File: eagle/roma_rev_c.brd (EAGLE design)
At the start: 49 x 41 mm, 23 parts, among them IC1 78L12, U1 LTC3426

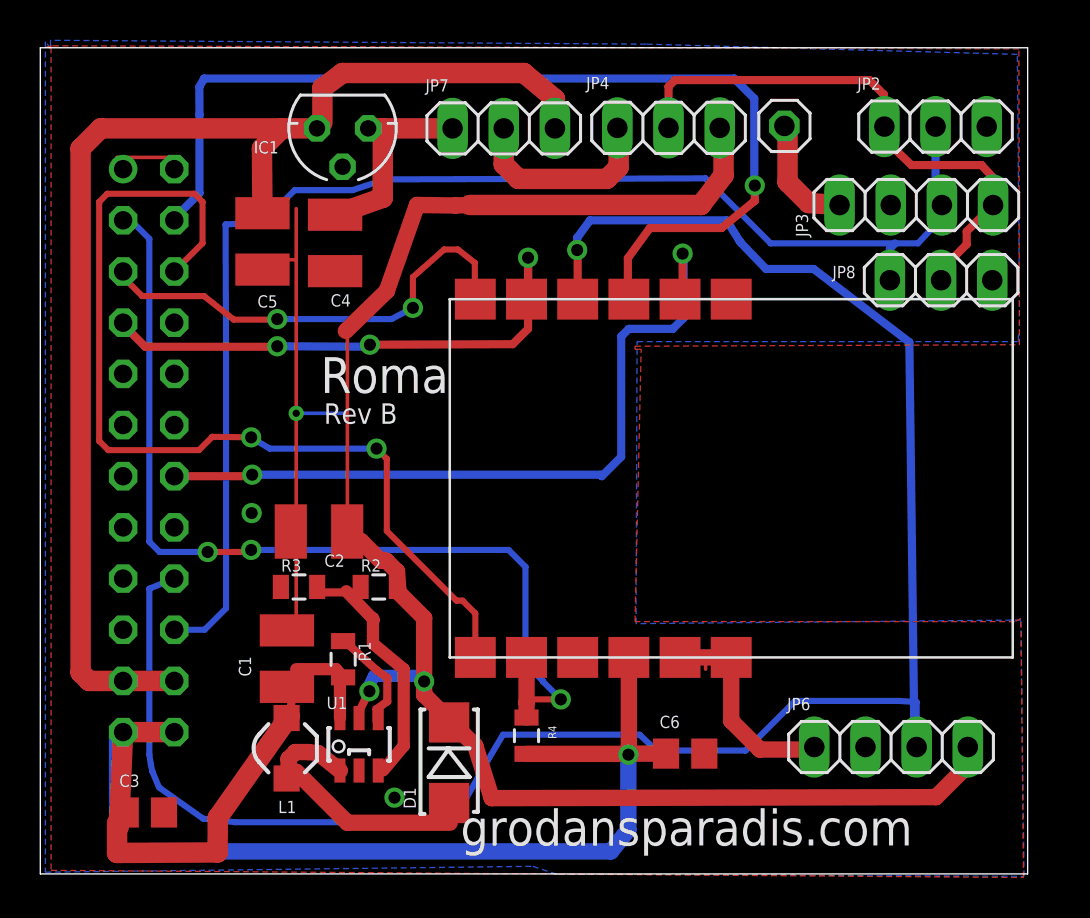
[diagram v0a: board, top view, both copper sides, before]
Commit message: JP4 should be numbered the other way around. Added descriptive text.
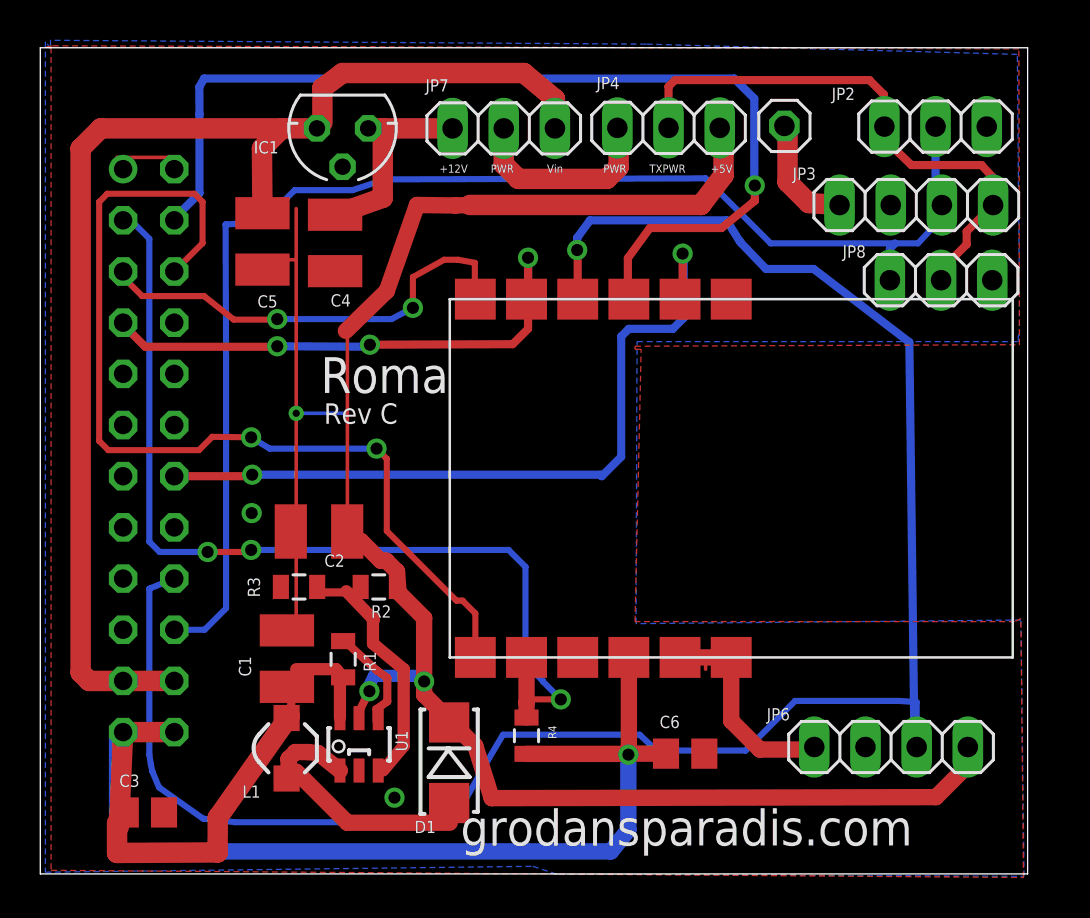
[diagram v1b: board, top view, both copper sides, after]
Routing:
- net SCK1: track 22.8 -> 22.2 mm
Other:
- board text added: "+12V"
- board text added: "+5V"
- board text added: "PWR"
- board text added: "Rev C"
- board text added: "TXPWR"
- board text added: "Vin"
- board text removed: "Rev B"

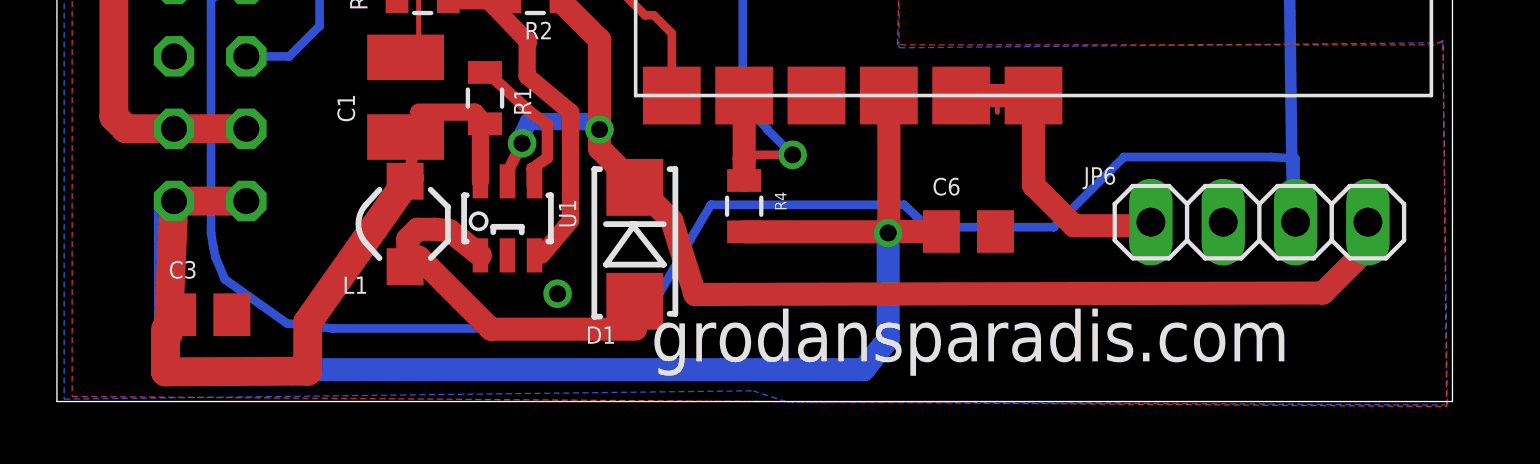
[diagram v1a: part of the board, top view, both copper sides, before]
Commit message: Added solder short to get +5V from Odessa 5V without converter.
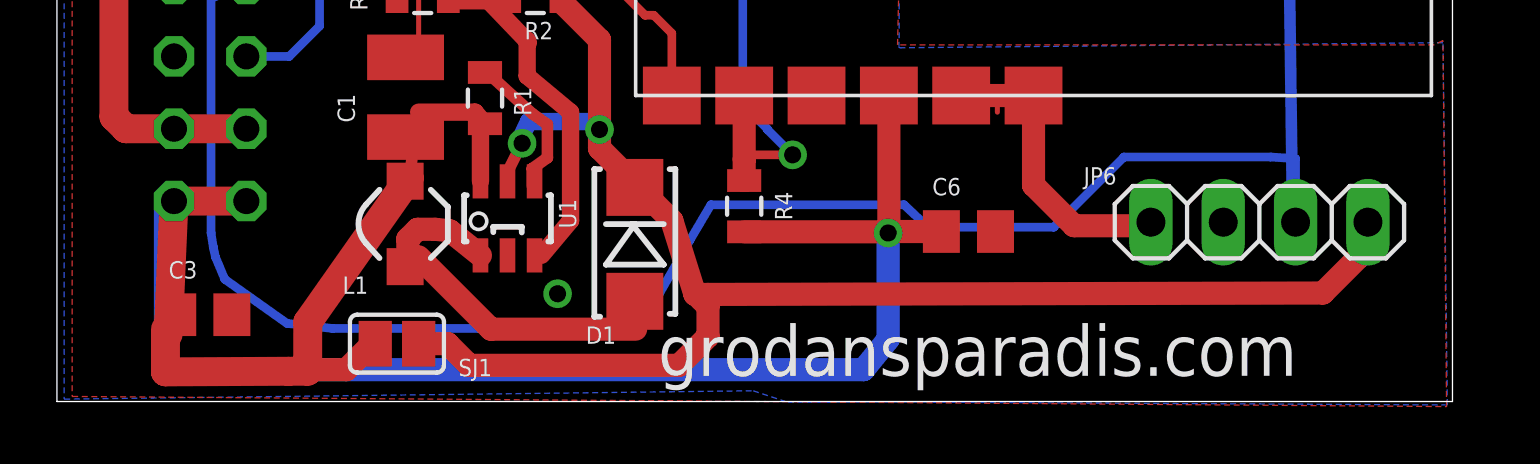
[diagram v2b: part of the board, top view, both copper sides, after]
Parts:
- added SJ1: (no value), jumper:SJ
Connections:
- net +3V3: now also SJ1.1
- net +5V: now also SJ1.2
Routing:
- net +5V: track 82.8 -> 95.8 mm
- net +3V3: track 77.9 -> 81.3 mm
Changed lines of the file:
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@@
 <plain>
 <text x="14.0759" y="22.339" size="1.016" layer="25" font="fixed">Rev C</text>
-<text x="20.8556" y="1.41" size="1.778" layer="25" font="fixed">grodansparadis.com</text>
+<text x="21.1096" y="0.902" size="1.778" layer="25" font="fixed">grodansparadis.com</text>
 <text x="13.9129" y="23.8682" size="1.778" layer="25" font="fixed">Roma</text>
 <wire x1="0" y1="0" x2="0" y2="41" width="0" layer="20"/>
@@
 <element name="U$1" library="eurosource_mrf24j40ma" package="MRF24J40MA" value="MRF24J40MA" x="27.94" y="19.6342" smashed="yes" rot="R270"/>
 <element name="R4" library="CH_passive" package="0805" value="10K" x="24.13" y="6.858" smashed="yes" rot="R270">
-<attribute name="NAME" x="25.2095" y="7.366" size="0.4064" layer="25" rot="R270"/>
+<attribute name="NAME" x="25.2095" y="7.366" size="0.6096" layer="25" rot="R270"/>
 </element>
 <element name="C6" library="rcl" package="C0805" value="100n" x="32.004" y="5.969" smashed="yes">
@@
 <attribute name="NAME" x="40.9702" y="31.1912" size="0.6096" layer="25" ratio="10" rot="R180"/>
 <attribute name="VALUE" x="40.894" y="26.289" size="1.27" layer="27"/>
+</element>
+<element name="SJ1" library="jumper" package="SJ" value="" x="11.938" y="2.032" smashed="yes">
+<attribute name="NAME" x="14.097" y="0.889" size="0.6096" layer="25" ratio="10"/>
+<attribute name="VALUE" x="12.3381" y="2.032" size="0.02" layer="27"/>
 </element>
 </elements>
@@
 <wire x1="8.8065" y1="2.7863" x2="12.3698" y2="7.8486" width="1.016" layer="1"/>
 <wire x1="8.8019" y1="1.0651" x2="8.8065" y2="2.7863" width="1.016" layer="1"/>
-<wire x1="3.81" y1="1.0413" x2="8.8019" y2="1.0651" width="1.016" layer="1"/>
+<wire x1="3.81" y1="1.0413" x2="8.12778125" y2="1.0618875" width="1.016" layer="1"/>
+<wire x1="8.12778125" y1="1.0618875" x2="8.8019" y2="1.0651" width="1.016" layer="1"/>
 <wire x1="3.81" y1="2.54" x2="3.81" y2="1.0413" width="1.016" layer="1"/>
 <wire x1="12.3698" y1="7.8486" x2="12.2249" y2="7.7357" width="1.016" layer="1"/>
@@
 <wire x1="24.13" y1="5.958" x2="29.1448" y2="5.958" width="0.8128" layer="1"/>
 <wire x1="29.1448" y1="5.958" x2="29.1846" y2="5.9182" width="0.8128" layer="1"/>
+<contactref element="SJ1" pad="1"/>
+<wire x1="11.176" y1="2.032" x2="11.0744" y2="2.032" width="0.8128" layer="1"/>
+<wire x1="11.0744" y1="2.032" x2="10.16" y2="1.1176" width="0.8128" layer="1"/>
+<wire x1="10.16" y1="1.1176" x2="8.18349375" y2="1.1176" width="0.8128" layer="1"/>
+<wire x1="8.18349375" y1="1.1176" x2="8.12778125" y2="1.0618875" width="0.8128" layer="1"/>
 </signal>
 <signal name="N$2">
@@
 <wire x1="17.78" y1="13.97" x2="17.697" y2="14.2419" width="0.1778" layer="1"/>
 <wire x1="44.45" y1="3.81" x2="45.72" y2="5.08" width="0.8128" layer="1"/>
-<wire x1="22.4028" y1="3.7592" x2="44.45" y2="3.81" width="0.8128" layer="1"/>
+<wire x1="22.4028" y1="3.7592" x2="22.860115625" y2="3.760253125" width="0.8128" layer="1"/>
+<wire x1="22.860115625" y1="3.760253125" x2="44.45" y2="3.81" width="0.8128" layer="1"/>
 <wire x1="21.59" y1="6.35" x2="22.4028" y2="3.7592" width="0.8128" layer="1"/>
 <wire x1="20.32" y1="7.62" x2="21.59" y2="6.35" width="0.8128" layer="1"/>
@@
 <wire x1="16.2521" y1="8.9193" x2="15.7949" y2="8.01" width="0.4064" layer="1"/>
 <wire x1="15.7949" y1="8.01" x2="15.8203" y2="7.7306" width="0.4064" layer="1"/>
+<contactref element="SJ1" pad="2"/>
+<wire x1="12.7" y1="2.032" x2="13.716" y2="2.032" width="0.8128" layer="1"/>
+<wire x1="13.716" y1="2.032" x2="14.478" y2="1.27" width="0.8128" layer="1"/>
+<wire x1="14.478" y1="1.27" x2="21.844" y2="1.27" width="0.8128" layer="1"/>
+<wire x1="21.844" y1="1.27" x2="22.86" y2="2.286" width="0.8128" layer="1"/>
+<wire x1="22.86" y1="2.286" x2="22.86" y2="3.34369375" width="0.8128" layer="1"/>
+<wire x1="22.86" y1="3.34369375" x2="22.626846875" y2="3.576846875" width="0.8128" layer="1"/>
+<wire x1="22.626846875" y1="3.576846875" x2="22.3837375" y2="3.81995625" width="0.8128" layer="1"/>
+<wire x1="22.86" y1="3.81" x2="22.626846875" y2="3.576846875" width="0.1778" layer="1"/>
+<wire x1="22.86" y1="3.81" x2="22.860115625" y2="3.760253125" width="0.1778" layer="1"/>
 </signal>
 <signal name="N$4">

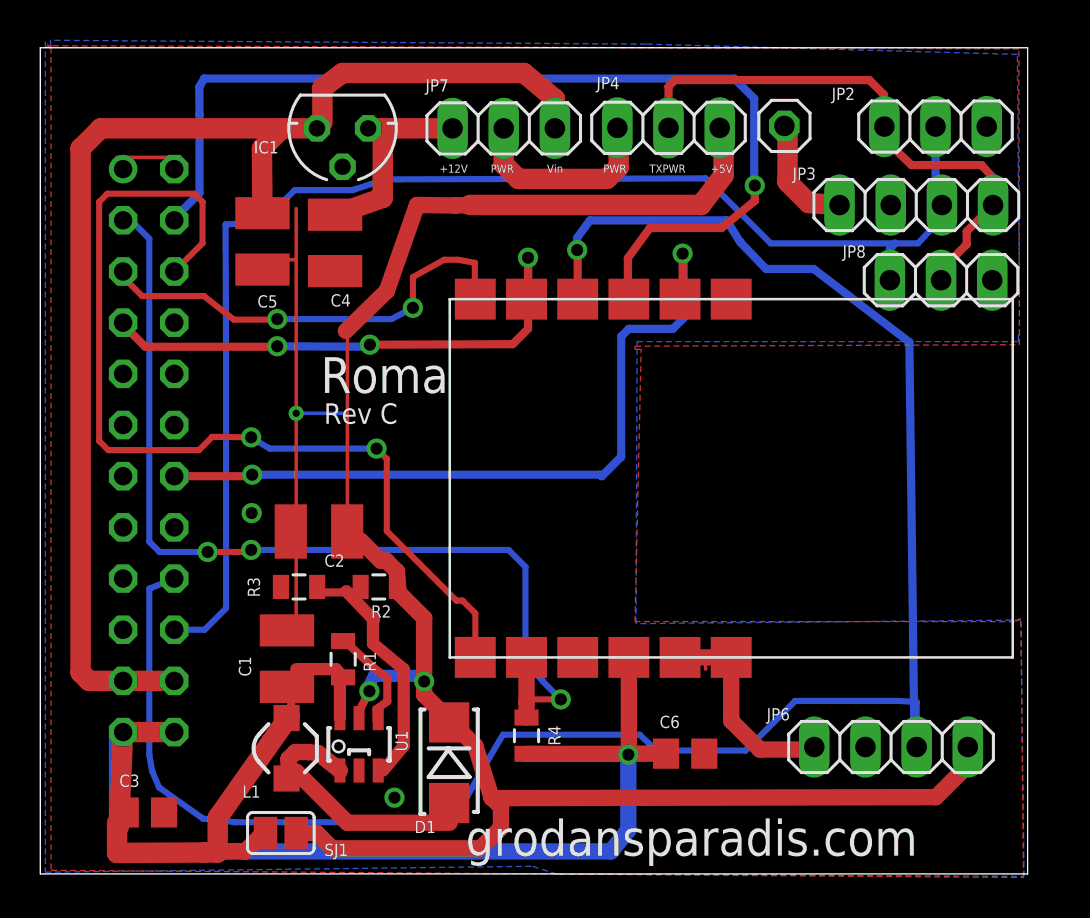
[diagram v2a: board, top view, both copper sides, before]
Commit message: Redrawn signal that goes over transceiver protected zone
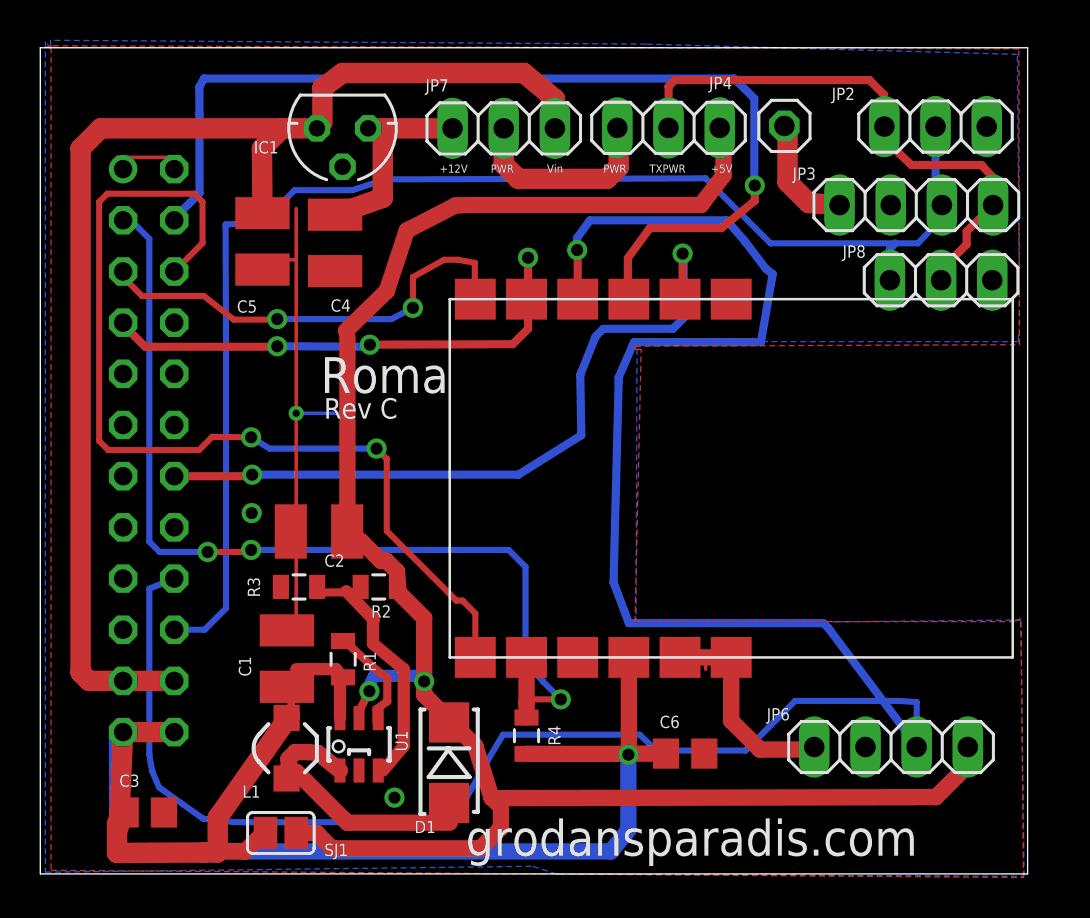
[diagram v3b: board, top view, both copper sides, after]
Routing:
- net RX_433: track 97.9 -> 111.2 mm
- net RESET: track 37.6 -> 36.1 mm
- net +5V: track 95.8 -> 95.2 mm
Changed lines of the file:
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@@
 <board>
 <plain>
-<text x="14.0759" y="22.339" size="1.016" layer="25" font="fixed">Rev C</text>
+<text x="14.0759" y="22.593" size="1.016" layer="25" font="fixed">Rev C</text>
 <text x="21.1096" y="0.902" size="1.778" layer="25" font="fixed">grodansparadis.com</text>
 <text x="13.9129" y="23.8682" size="1.778" layer="25" font="fixed">Roma</text>
@@
 </element>
 <element name="JP4" library="pinhead" package="1X03" value="" x="31.1785" y="37.0242" smashed="yes" rot="R180">
-<attribute name="NAME" x="27.5971" y="38.9472" size="0.6096" layer="25" ratio="10"/>
+<attribute name="NAME" x="33.1851" y="38.9472" size="0.6096" layer="25" ratio="10"/>
 <attribute name="VALUE" x="34.9885" y="40.1992" size="1.27" layer="27" rot="R180"/>
 </element>
@@
 </element>
 <element name="C4" library="CH_passive" package="1210" value="22uF" x="14.6312" y="31.3142" smashed="yes" rot="R270">
-<attribute name="NAME" x="14.4058" y="28.1582" size="0.6096" layer="25"/>
+<attribute name="NAME" x="14.4058" y="27.9042" size="0.6096" layer="25"/>
 </element>
 <element name="C5" library="CH_passive" package="1210" value="10uF" x="11.0254" y="31.3904" smashed="yes" rot="R270">
-<attribute name="NAME" x="10.7736" y="28.1084" size="0.6096" layer="25"/>
+<attribute name="NAME" x="9.7576" y="27.8544" size="0.6096" layer="25"/>
 </element>
 <element name="JP7" library="pinhead" package="1X03" value="" x="23" y="37" smashed="yes">
@@
 <contactref element="JP4" pad="1"/>
 <contactref element="JP6" pad="4"/>
-<wire x1="21.3106" y1="33.1978" x2="32.7914" y2="33.1978" width="1.016" layer="1"/>
-<wire x1="32.7914" y1="33.1978" x2="33.909" y2="34.671" width="1.016" layer="1"/>
-<wire x1="33.909" y1="34.671" x2="33.909" y2="36.8337" width="1.016" layer="1"/>
+<wire x1="21.3106" y1="33.1978" x2="32.7914" y2="33.1978" width="0.8128" layer="1"/>
+<wire x1="32.7914" y1="33.1978" x2="33.909" y2="34.671" width="0.8128" layer="1"/>
+<wire x1="33.909" y1="34.671" x2="33.909" y2="36.8337" width="0.8128" layer="1"/>
 <wire x1="33.909" y1="36.8337" x2="33.7185" y2="37.0242" width="0.4064" layer="1"/>
 <wire x1="17.78" y1="13.97" x2="17.7038" y2="15.0114" width="0.8128" layer="1"/>
@@
 <wire x1="15.24" y1="16.51" x2="15.2324" y2="16.9942" width="0.1778" layer="1"/>
 <wire x1="21.3106" y1="33.1978" x2="20.5994" y2="33.1724" width="0.8128" layer="1"/>
-<wire x1="20.5994" y1="33.1724" x2="18.6944" y2="33.1978" width="0.8128" layer="1"/>
-<wire x1="18.6944" y1="33.1978" x2="17.1958" y2="28.9306" width="0.8128" layer="1"/>
+<wire x1="20.5994" y1="33.1724" x2="18.1864" y2="31.9278" width="0.8128" layer="1"/>
+<wire x1="18.1864" y1="31.9278" x2="17.1958" y2="28.9306" width="0.8128" layer="1"/>
 <wire x1="17.1958" y1="28.9306" x2="15.1638" y2="26.9494" width="0.8128" layer="1"/>
 <wire x1="15.1638" y1="16.9612" x2="15.2324" y2="16.9942" width="0.8128" layer="1"/>
@@
 <wire x1="18.7706" y1="9.8298" x2="19.05" y2="9.5504" width="0.6096" layer="16"/>
 <via x="19.05" y="9.5504" extent="1-16" drill="0.6"/>
-<wire x1="15.24" y1="17.78" x2="15.24" y2="26.67" width="0.1778" layer="1"/>
+<wire x1="15.24" y1="17.78" x2="15.24" y2="26.67" width="0.8128" layer="1"/>
 <wire x1="15.24" y1="26.67" x2="15.1638" y2="26.9494" width="0.1778" layer="1"/>
 <wire x1="15.24" y1="17.78" x2="15.2324" y2="16.9942" width="0.1778" layer="1"/>
@@
 <wire x1="26.6446" y1="31.5722" x2="27.2796" y2="32.4358" width="0.4064" layer="16"/>
 <wire x1="27.2796" y1="32.4358" x2="34.0614" y2="32.4358" width="0.4064" layer="16"/>
-<wire x1="34.0614" y1="32.4358" x2="34.6964" y2="31.4198" width="0.4064" layer="16"/>
-<wire x1="34.6964" y1="31.4198" x2="34.7726" y2="31.3182" width="0.4064" layer="16"/>
-<wire x1="34.7726" y1="31.3182" x2="36.0172" y2="30.0228" width="0.4064" layer="16"/>
-<wire x1="36.0172" y1="30.0228" x2="38.3794" y2="30.0228" width="0.4064" layer="16"/>
-<wire x1="38.3794" y1="30.0228" x2="43.1292" y2="26.3906" width="0.4064" layer="16"/>
-<wire x1="43.1292" y1="26.3906" x2="43.3832" y2="6.5069" width="0.4064" layer="16"/>
+<wire x1="34.0614" y1="32.4358" x2="34.9504" y2="31.4198" width="0.4064" layer="16"/>
+<wire x1="34.9504" y1="31.4198" x2="35.0266" y2="31.3182" width="0.4064" layer="16"/>
+<wire x1="35.0266" y1="31.3182" x2="36.0172" y2="30.0228" width="0.4064" layer="16"/>
+<wire x1="36.0172" y1="30.0228" x2="36.3474" y2="29.7688" width="0.4064" layer="16"/>
+<wire x1="36.3474" y1="29.7688" x2="35.7632" y2="26.3906" width="0.4064" layer="16"/>
+<wire x1="35.7632" y1="26.3906" x2="29.464" y2="26.3906" width="0.4064" layer="16"/>
+<wire x1="29.464" y1="26.3906" x2="28.702" y2="24.638" width="0.4064" layer="16"/>
+<wire x1="28.702" y1="24.638" x2="28.702" y2="24.384" width="0.4064" layer="16"/>
+<wire x1="28.702" y1="24.384" x2="28.448" y2="14.478" width="0.4064" layer="16"/>
+<wire x1="28.448" y1="14.478" x2="29.21" y2="12.446" width="0.4064" layer="16"/>
+<wire x1="29.21" y1="12.446" x2="38.862" y2="12.446" width="0.4064" layer="16"/>
+<wire x1="38.862" y1="12.446" x2="39.116" y2="12.192" width="0.4064" layer="16"/>
+<wire x1="39.116" y1="12.192" x2="43.3832" y2="6.5069" width="0.4064" layer="16"/>
 <wire x1="43.3832" y1="6.5069" x2="43.4911" y2="6.2974" width="0.4064" layer="16"/>
 </signal>
@@
 <contactref element="U$1" pad="2"/>
 <contactref element="JP1" pad="14"/>
-<wire x1="27.8654" y1="19.7374" x2="28.829" y2="20.701" width="0.4064" layer="16"/>
-<wire x1="28.829" y1="20.701" x2="28.829" y2="26.67" width="0.4064" layer="16"/>
-<wire x1="28.829" y1="26.67" x2="29.21" y2="27.051" width="0.4064" layer="16"/>
-<wire x1="29.21" y1="27.051" x2="31.3944" y2="27.051" width="0.4064" layer="16"/>
+<wire x1="26.8494" y1="21.7694" x2="26.797" y2="24.765" width="0.4064" layer="16"/>
+<wire x1="26.797" y1="24.765" x2="27.559" y2="26.67" width="0.4064" layer="16"/>
+<wire x1="27.559" y1="26.67" x2="27.94" y2="27.051" width="0.4064" layer="16"/>
+<wire x1="27.94" y1="27.051" x2="31.3944" y2="27.051" width="0.4064" layer="16"/>
 <wire x1="31.3944" y1="27.051" x2="31.9278" y2="27.5844" width="0.4064" layer="16"/>
 <wire x1="31.9278" y1="27.5844" x2="31.9278" y2="30.734" width="0.4064" layer="16"/>
@@
 <wire x1="10.441" y1="19.7374" x2="10.5156" y2="19.812" width="0.4064" layer="1"/>
 <via x="10.5156" y="19.812" extent="1-16" drill="0.6"/>
-<wire x1="10.5156" y1="19.812" x2="27.7908" y2="19.812" width="0.4064" layer="16"/>
-<wire x1="27.7908" y1="19.812" x2="27.8654" y2="19.7374" width="0.4064" layer="16"/>
+<wire x1="10.5156" y1="19.812" x2="23.7268" y2="19.812" width="0.4064" layer="16"/>
+<wire x1="23.7268" y1="19.812" x2="26.8494" y2="21.7694" width="0.4064" layer="16"/>
 </signal>
 <signal name="CS_MRF24J40MA">
